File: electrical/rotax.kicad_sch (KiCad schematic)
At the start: 19 parts

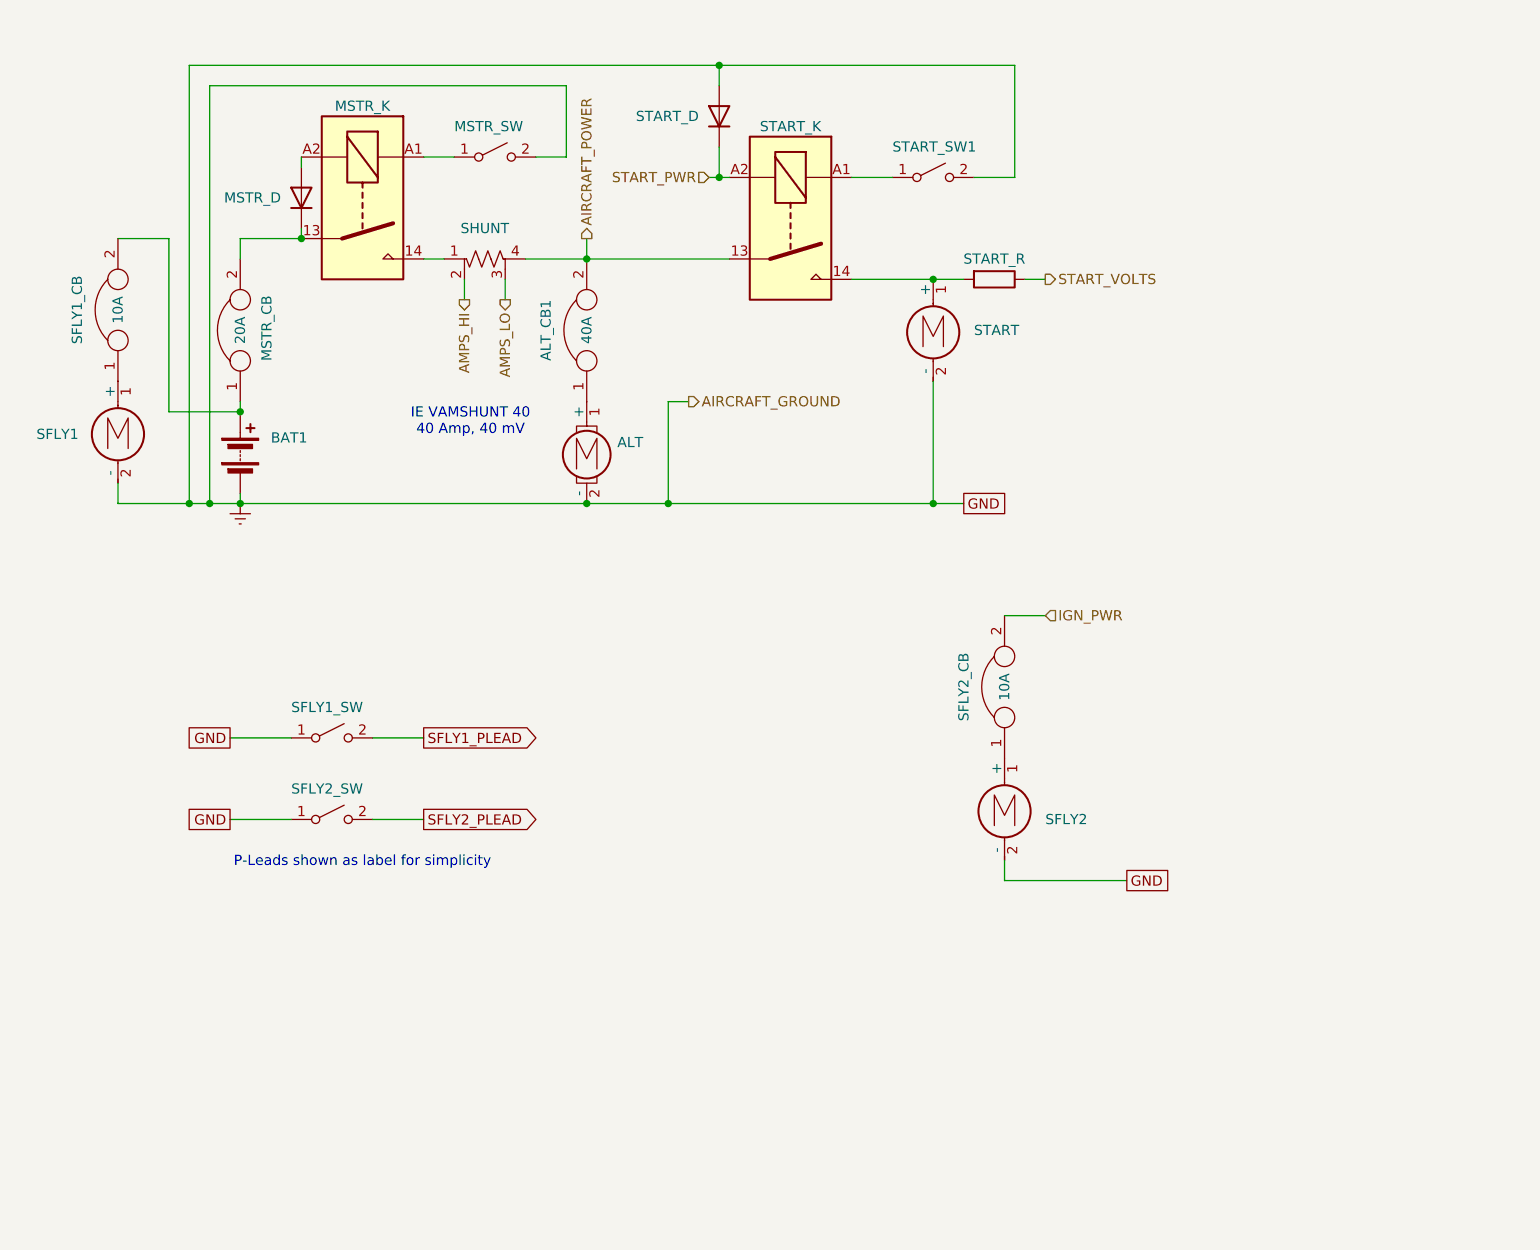
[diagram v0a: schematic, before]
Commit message: Changed contactors to be positive switched. Changed some CB's to Fuses for SureFly and main power. Added Fuel Pump.
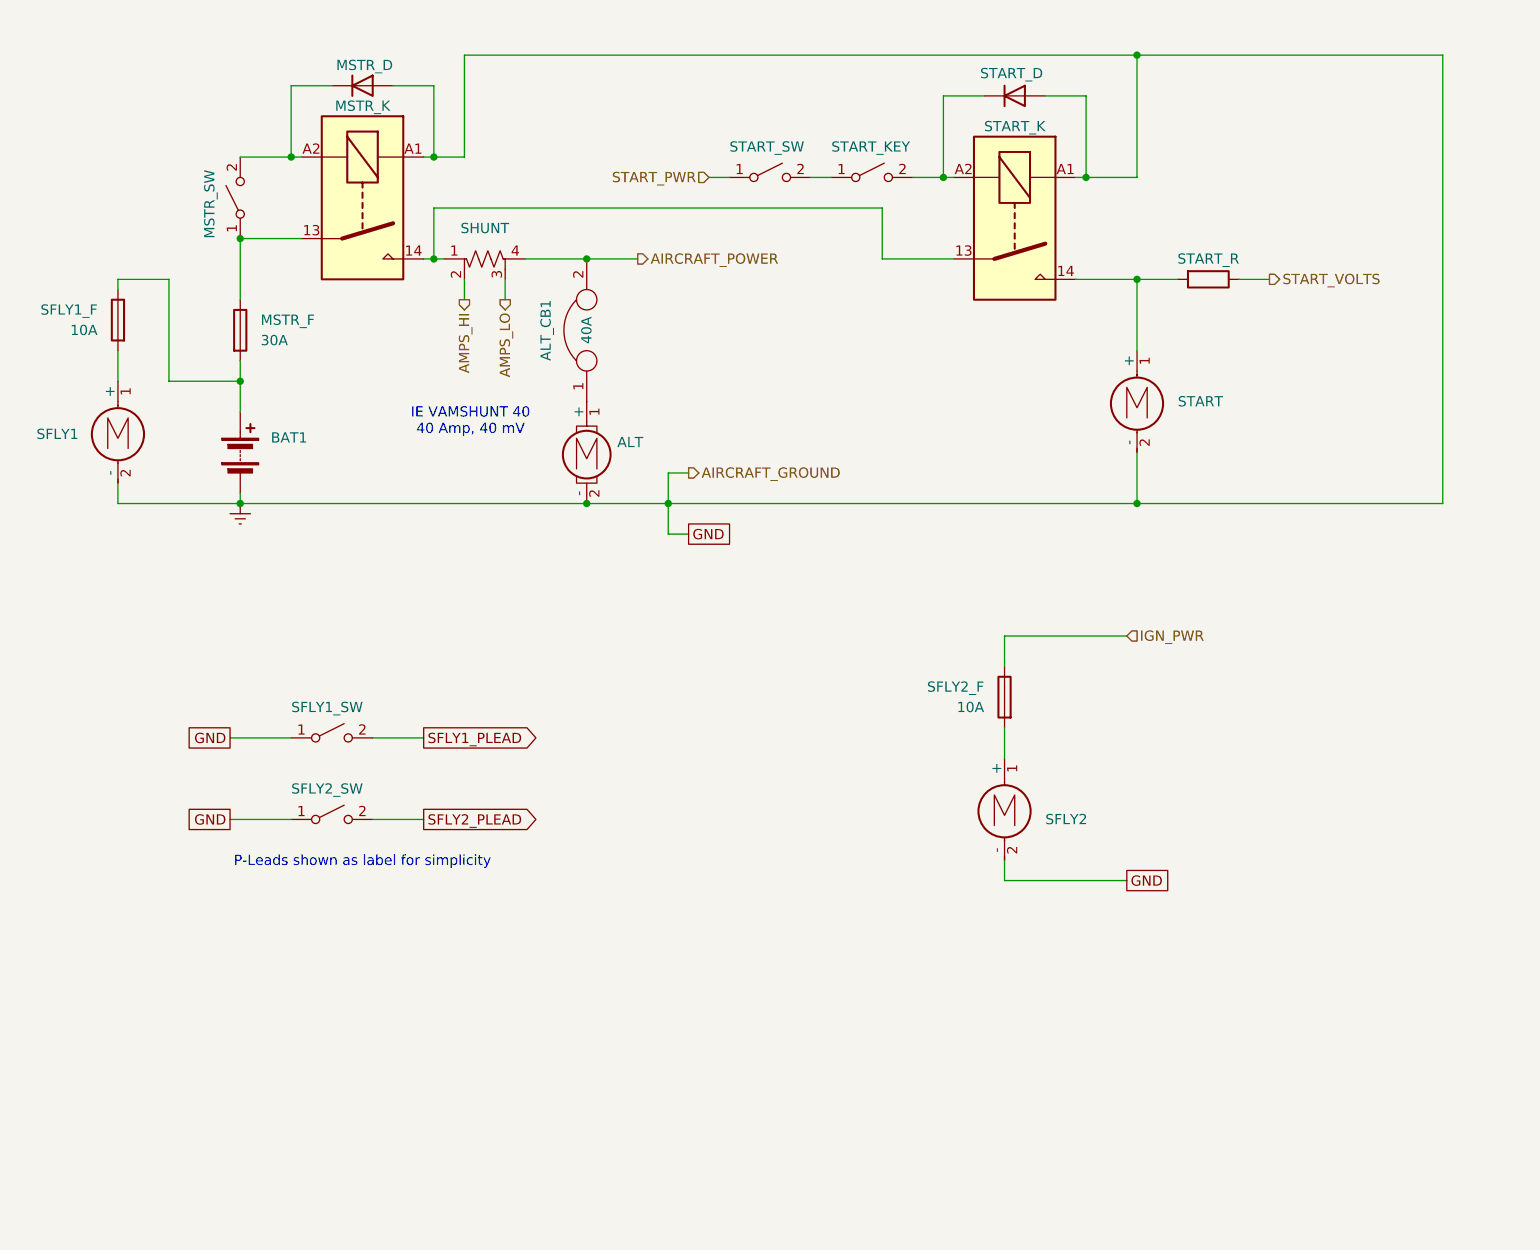
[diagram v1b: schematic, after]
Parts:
- removed MSTR_CB: 20A, symbol flyerx:Circuit_Breaker
- removed SFLY1_CB, SFLY2_CB: 10A, symbol flyerx:Circuit_Breaker
- added MSTR_F: 30A, symbol Device:Fuse
- added SFLY1_F, SFLY2_F: 10A, symbol Device:Fuse
- added START_KEY: ~, symbol Switch:SW_SPST
- renumbered START_SW1 to START_SW
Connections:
- net AIRCRAFT_POWER: no longer START_K.13
- net Earth: now also MSTR_D.2 (A), MSTR_K.A1, START_K.A1; no longer MSTR_SW.2 (B), START_SW.2 (B)
- net IGN_PWR: now also SFLY2_F.1
- net START_PWR: now also START_SW.1 (A); no longer START_D.1 (K), START_K.A2
- net at MSTR_D.1 (K): now also MSTR_K.A2, MSTR_SW.2 (B); no longer MSTR_K.13
- net at SFLY1.1 (+): now also SFLY1_F.2
- net at BAT1.1 (+): now also MSTR_F.2, SFLY1_F.1
- net at MSTR_K.14, SHUNT.1: now also START_K.13
- net at MSTR_SW.1 (A): now also MSTR_K.13, MSTR_F.1; no longer MSTR_K.A1
- net at SFLY2.1 (+): now also SFLY2_F.2
- new net: START_KEY.1 (A), START_SW.2 (B)
- new net: START_D.1 (K), START_K.A2, START_KEY.2 (B)
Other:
- moved on the sheet: MSTR_D, MSTR_SW, START, START_D, START_K, START_R, START_SW

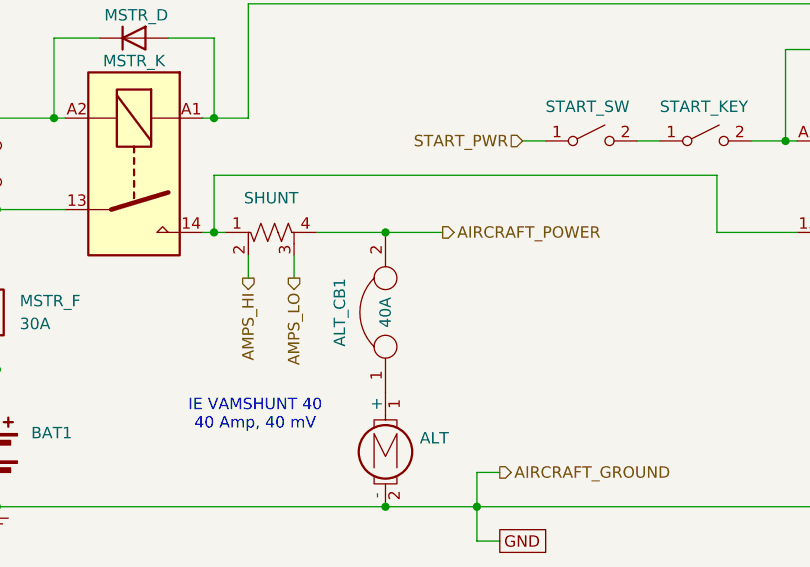
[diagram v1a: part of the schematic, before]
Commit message: Changed power outputs on VP-X to match sides the LRU's are on. Also, removed Shunt from wiring and just use VP-X for Amperage.
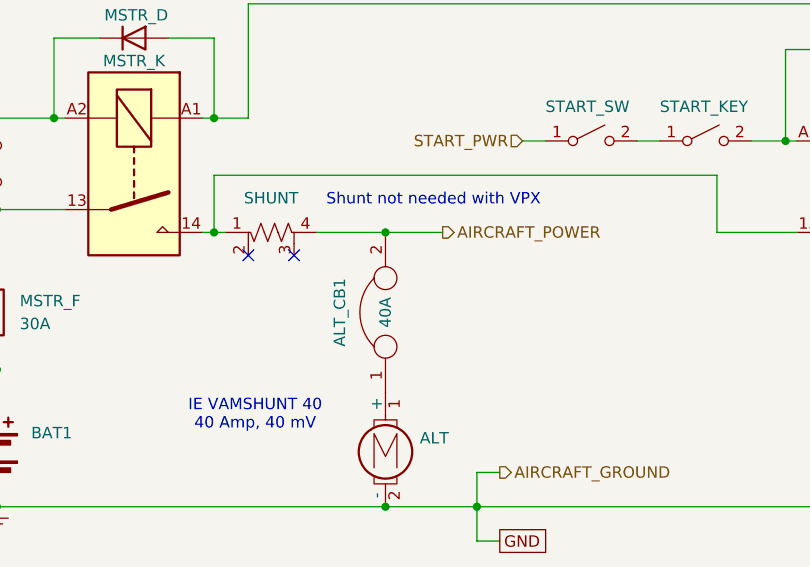
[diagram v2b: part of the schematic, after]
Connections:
- net AMPS_HI: no longer names the net of SHUNT.2
- net AMPS_LO: no longer names the net of SHUNT.3
- no-connect marks 0 -> 2
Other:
- note added: "Shunt not needed with VPX"
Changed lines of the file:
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@@
 	(title_block
 		(title "Lycoming")
-		(date "2025-09-25")
-		(rev "1.0.5")
+		(date "2025-09-29")
+		(rev "1.0.7")
 		(company "N78HR")
+	)
+	(text "Shunt not needed with VPX"
+		(exclude_from_sim no)
+		(at 91.694 40.894 0)
+		(effects
+			(font
+				(size 1.27 1.27)
+			)
+		)
 	)
 	(text "P-Leads shown as label for simplicity"
@@
 		(color 0 0 0 0)
 	)
+	(no_connect
+		(at 76.2 46.99)
+	)
+	(no_connect
+		(at 71.12 46.99)
+	)
 	(wire
 		(pts
@@
 	(wire
 		(pts
-			(xy 71.12 46.99) (xy 71.12 49.53)
-		)
-		(stroke
-			(width 0)
-			(type default)
-		)
-	)
-	(wire
-		(pts
 			(xy 59.69 104.14) (xy 66.04 104.14)
 		)
@@
 		(pts
 			(xy 148.59 24.13) (xy 148.59 34.29)
-		)
-		(stroke
-			(width 0)
-			(type default)
-		)
-	)
-	(wire
-		(pts
-			(xy 76.2 46.99) (xy 76.2 49.53)
 		)
 		(stroke
@@
 		)
 	)
-	(hierarchical_label "AMPS_HI"
-		(shape output)
-		(at 71.12 49.53 270)
-		(effects
-			(font
-				(size 1.27 1.27)
-			)
-			(justify right)
-		)
-	)
 	(hierarchical_label "START_PWR"
 		(shape input)
@@
 		)
 	)
-	(hierarchical_label "AMPS_LO"
-		(shape output)
-		(at 76.2 49.53 270)
-		(effects
-			(font
-				(size 1.27 1.27)
-			)
-			(justify right)
-		)
-	)

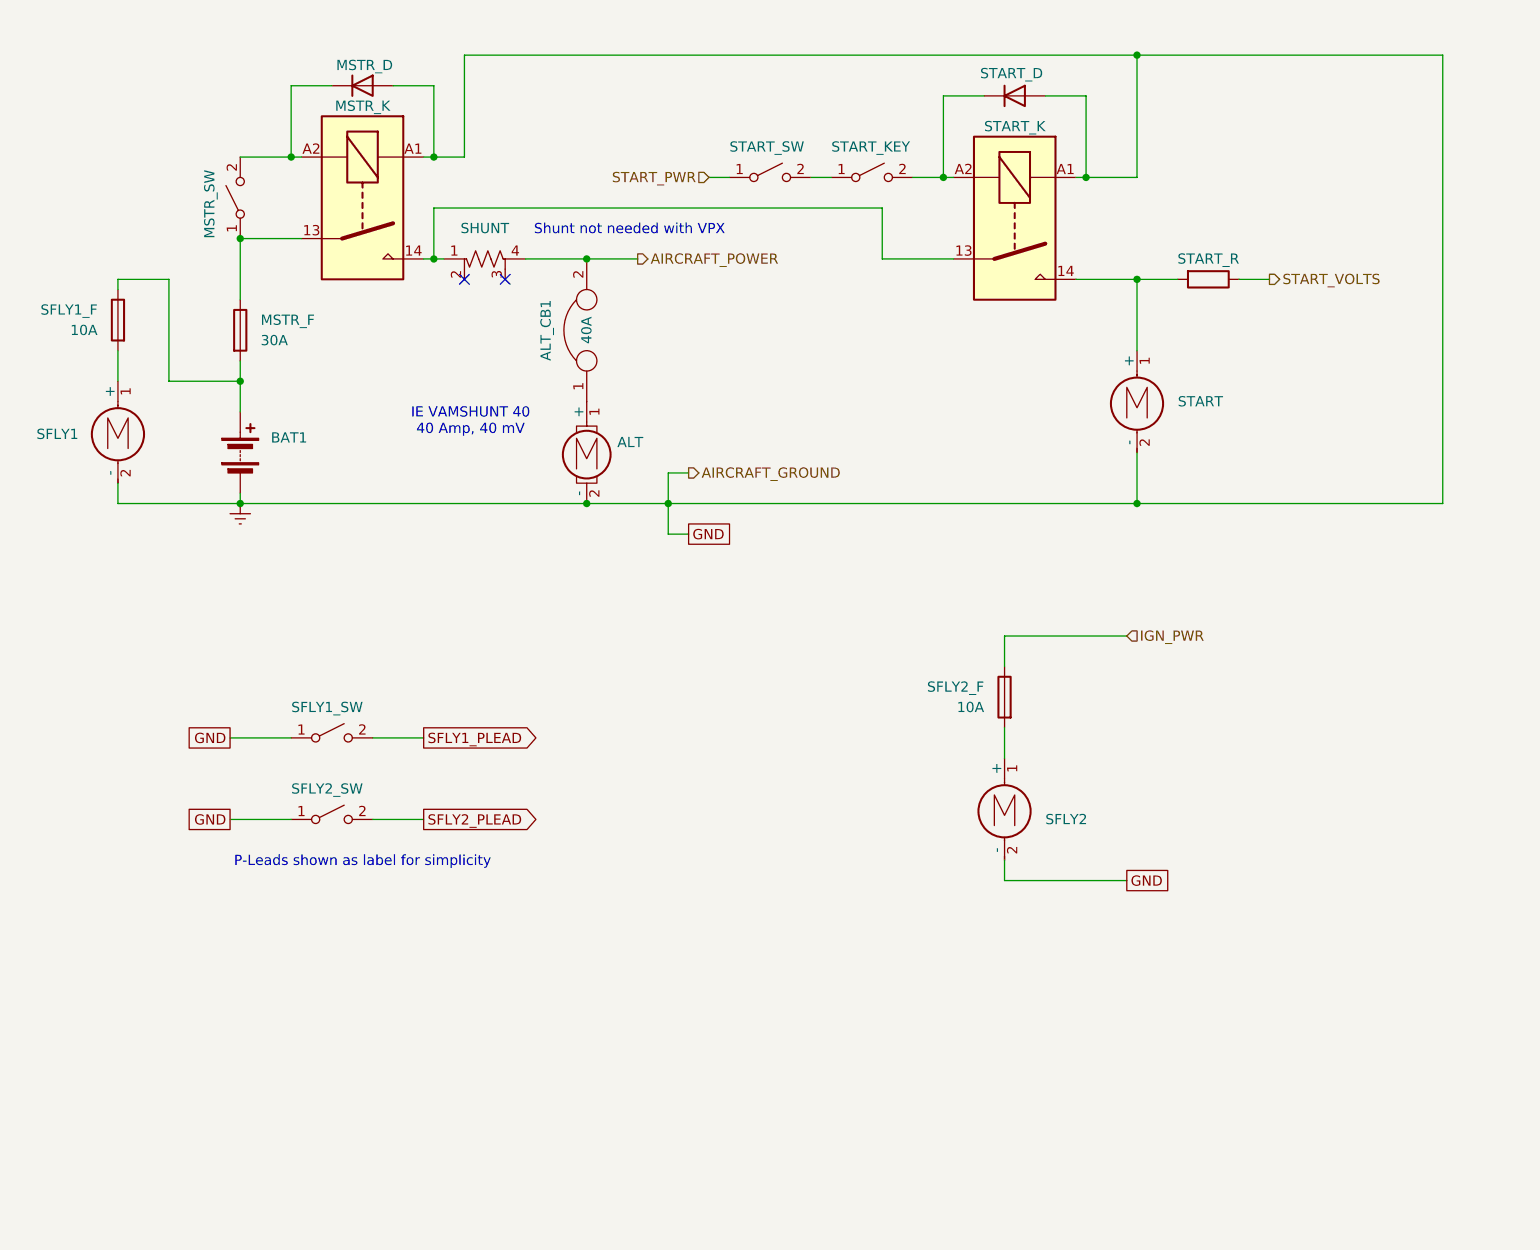
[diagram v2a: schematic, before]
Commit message: Added connectors and non-CAN/RS232/Ethernet shields.
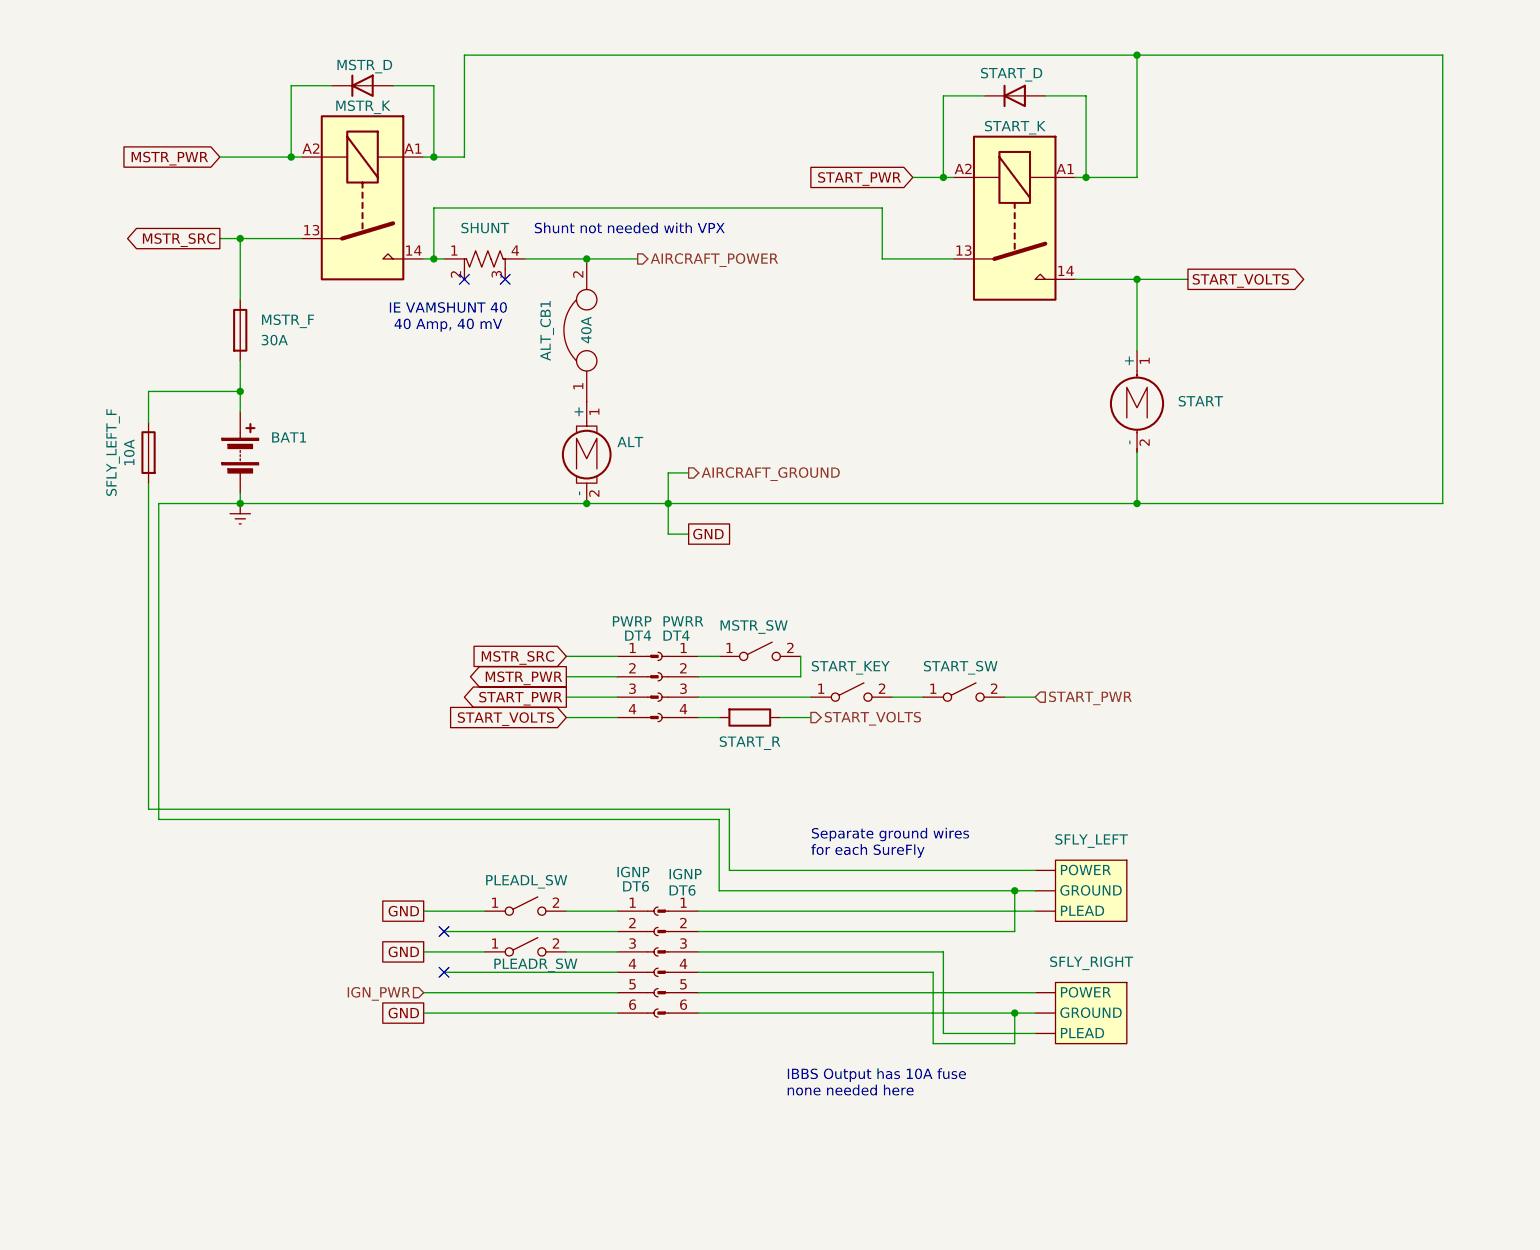
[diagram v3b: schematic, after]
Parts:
- removed SFLY1, SFLY2: Motor_DC, symbol Motor:Motor_DC
- removed SFLY2_F: 10A, symbol Device:Fuse
- added IGNP: DT6, symbol Connector:Conn_01x06_Pin
- added IGNP: DT6, symbol Connector:Conn_01x06_Socket
- added PWRP: DT4, symbol Connector:Conn_01x04_Pin
- added PWRR: DT4, symbol Connector:Conn_01x04_Socket
- added SFLY_LEFT, SFLY_RIGHT: ~, symbol flyerx:SureFly_SIM
- renumbered SFLY1_SW to PLEADL_SW, SFLY2_SW to PLEADR_SW, SFLY1_F to SFLY_LEFT_F
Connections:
- net Earth: now also IGNP.2 (Pin_2), IGNP.6 (Pin_6), SFLY_LEFT. (PLEAD)
- net IGN_PWR: now also IGNP.5 (Pin_5)
- net START_PWR: now also START_D.1 (K), START_K.A2, START_SW.2 (B), PWRP.3 (Pin_3); no longer START_SW.1 (A)
- net START_VOLTS: now also START.1 (+), START_K.14, PWRP.4 (Pin_4)
- net at START_KEY.1 (A): now also PWRR.3 (Pin_3); no longer START_SW.2 (B)
- net MSTR_PWR: now reaches MSTR_D.1 (K), MSTR_K.A2
- net MSTR_PWR: now also PWRP.2 (Pin_2); no longer MSTR_SW.2 (B)
- net MSTR_SRC: now reaches MSTR_F.1, MSTR_K.13
- net MSTR_SRC: now also PWRP.1 (Pin_1); no longer MSTR_SW.1 (A)
- net at SFLY_LEFT_F.2: now also SFLY_LEFT. (PLEAD)
- net SFLY1_PLEAD: no longer names the net of PLEADL_SW.2 (B)
- net SFLY1_PLEAD: now also IGNP.1 (Pin_1)
- net SFLY2_PLEAD: no longer names the net of PLEADR_SW.2 (B)
- net SFLY2_PLEAD: now also IGNP.3 (Pin_3)
- new net: MSTR_SW.1 (A), PWRR.1 (Pin_1)
- new net: MSTR_SW.2 (B), PWRR.2 (Pin_2)
- new net: PWRR.4 (Pin_4), START_R.2
- new net: START_KEY.2 (B), START_SW.1 (A)
- new net: IGNP.1 (Pin_1), SFLY_LEFT. (PLEAD)
- new net: IGNP.3 (Pin_3), SFLY_RIGHT. (PLEAD)
- new net: IGNP.4 (Pin_4), IGNP.6 (Pin_6), SFLY_RIGHT. (PLEAD)
- new net: IGNP.5 (Pin_5), SFLY_RIGHT. (PLEAD)
- no-connect marks 2 -> 4
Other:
- note added: "IBBS Output has 10A fuse none needed here"
- note added: "Separate ground wires for each SureFly"
- note removed: "P-Leads shown as label for simplicity"
- moved on the sheet: MSTR_SW, PLEADL_SW, PLEADR_SW, SFLY_LEFT_F, START_KEY, START_R, START_SW
